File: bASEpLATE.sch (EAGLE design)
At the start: 8 parts, among them IC1 TINY10P, U1 MC7805BD2T

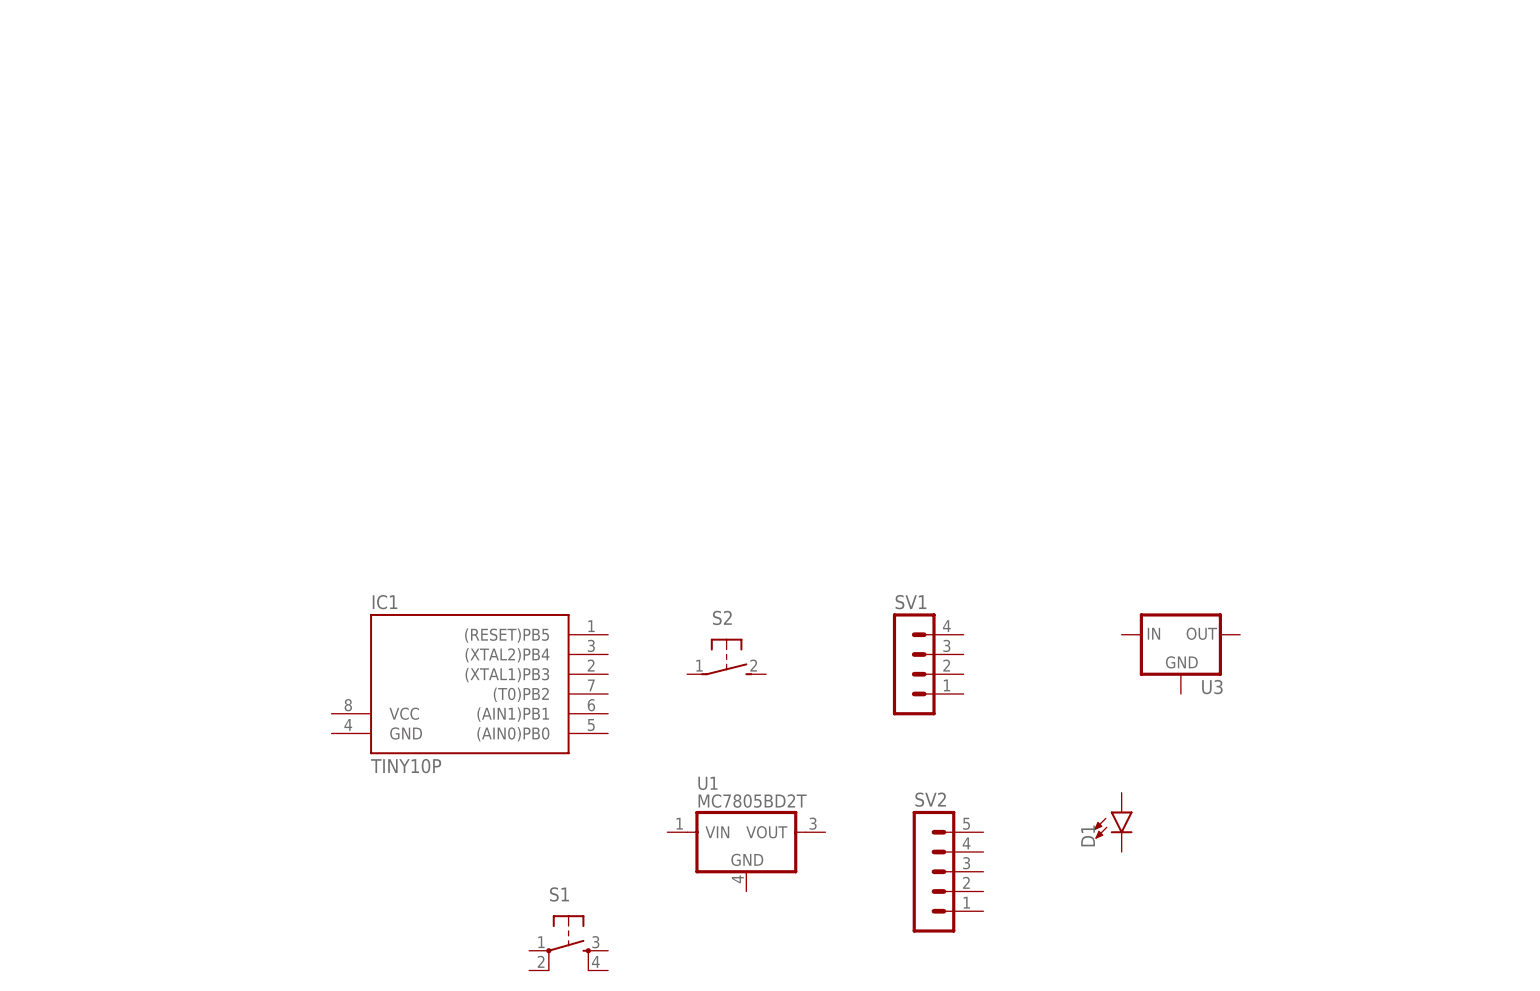
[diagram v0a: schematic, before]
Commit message: Switch Pulled High And 7805  mirrored
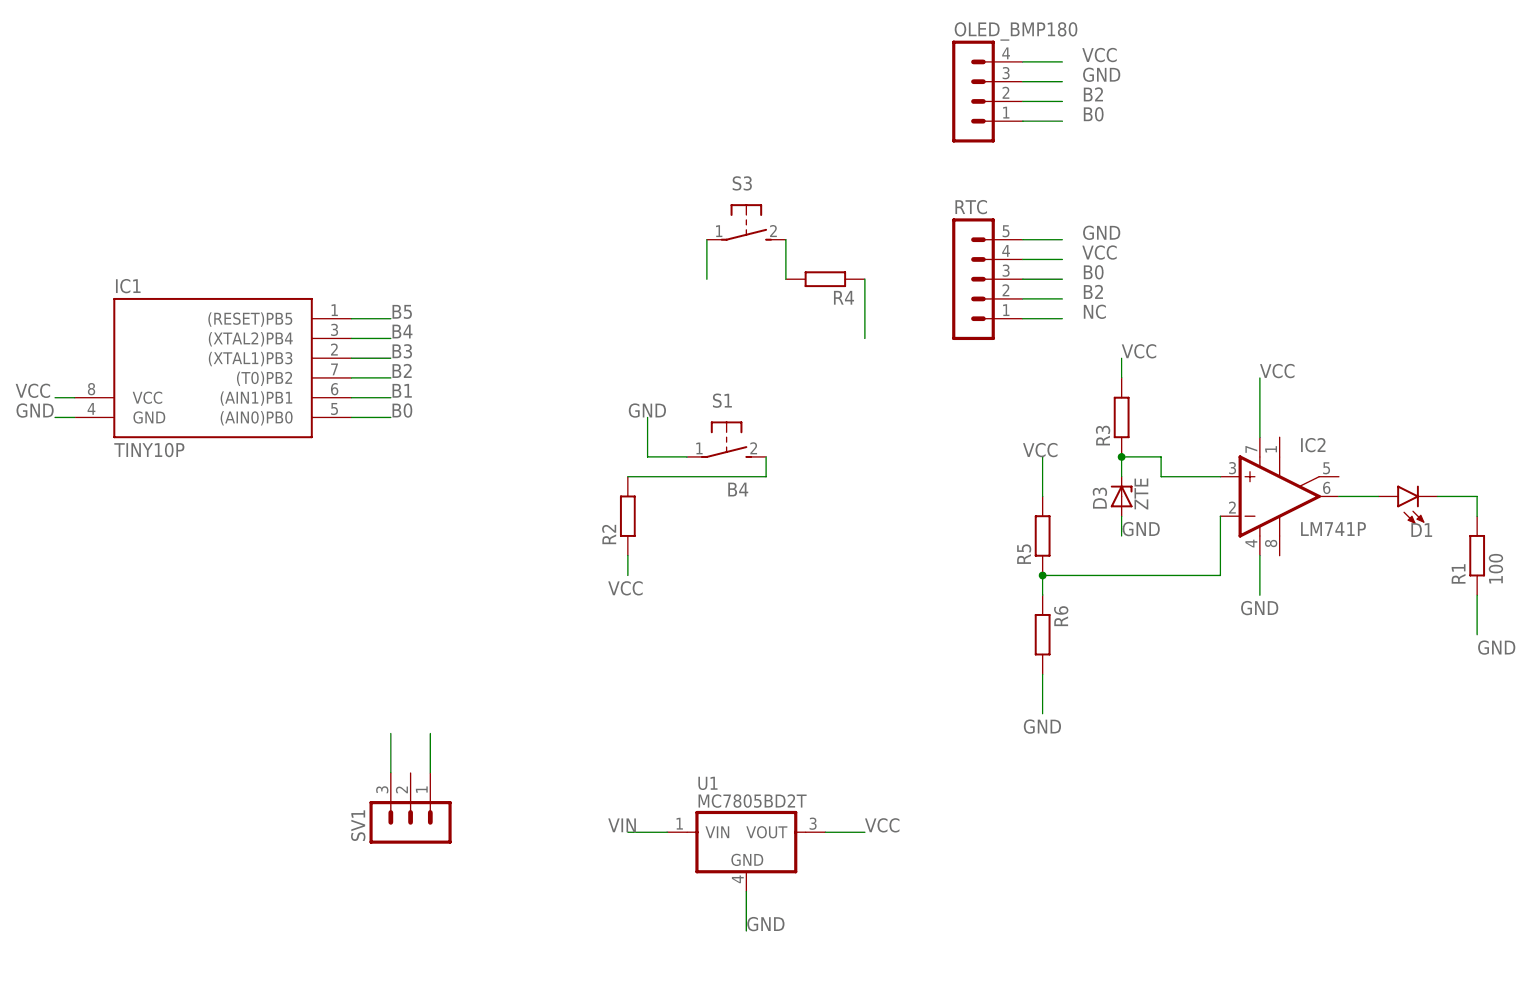
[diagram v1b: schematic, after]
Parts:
- removed S2: (no value), switch-omron:31-XX
- removed SV2: (no value), con-lstb:MA05-1
- removed U3: (no value), SparkFun-IC-Power:V_REG_78XX-TO-220
- added D3: ZTE, diode:ZTE
- added IC2: LM741P, linear:LM741P
- added OLED_BMP180: (no value), con-lstb:MA04-1
- added R1: 100, rcl:R-EU_0204/7
- added R2, R3, R4, R5, R6: (no value), rcl:R-EU_0204/7
- added RTC: (no value), con-lstb:MA05-1
- added S3: (no value), switch-omron:31-XX
- S1: device SparkFun-Retired:TAC_SWITCHPTH -> switch-omron:31-XX
- SV1: device con-lstb:MA04-1 -> con-lstb:MA03-1
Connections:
- new net B0: IC1.(AIN0)PB0, OLED_BMP180.1, RTC.3
- new net B1: IC1.(AIN1)PB1
- new net B2: IC1.(T0)PB2, OLED_BMP180.2, RTC.2
- new net B3: IC1.(XTAL1)PB3
- new net B4: IC1.(XTAL2)PB4, R2.2, S1.S
- new net B5: IC1.(RESET)PB5, R4.2, S3.S
- new net GND: D3.A, IC1.GND, IC2.V-, OLED_BMP180.3, R1.1, R6.2, RTC.5, S1.P, S3.P, SV1.3, U1.GND
- new net N$1: D1.A, IC2.OUT
- new net N$2: IC2.-IN, R5.1, R6.1
- new net N$3: D3.C, IC2.+IN, R3.1
- new net N$4: D1.C, R1.2
- new net NC: RTC.1
- new net VCC: IC1.VCC, IC2.V+, OLED_BMP180.4, R2.1, R3.2, R4.1, R5.2, RTC.4, U1.VOUT
- new net VIN: SV1.1, U1.VIN
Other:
- moved on the sheet: D1, IC1
